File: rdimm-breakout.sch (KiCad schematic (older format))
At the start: 2 parts

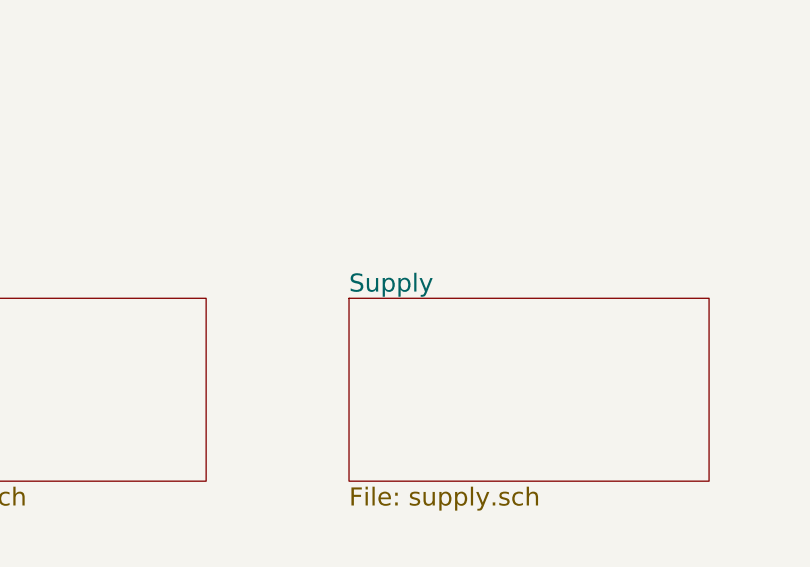
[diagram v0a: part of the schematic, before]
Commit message: Add FTDI and USB power supply
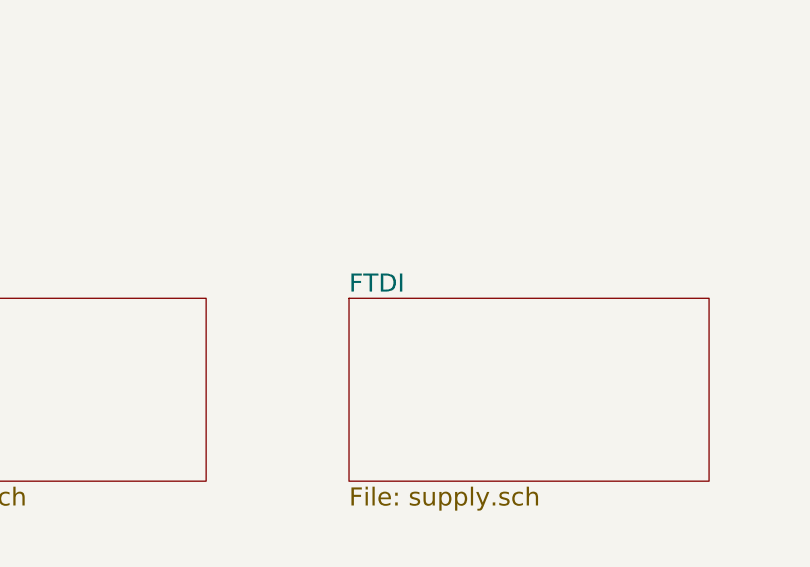
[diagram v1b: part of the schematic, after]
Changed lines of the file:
@@
 S 6975 6650 1575 800
 U 60225B0C
-F0 "Supply" 79
+F0 "FTDI" 79
 F1 "supply.sch" 79
 $EndSheet
